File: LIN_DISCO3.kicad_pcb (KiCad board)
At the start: 2 copper layers, 38.6 x 22.6 mm, 21 parts, among them J1 Conn_01x06_Female, U1 PIC16F628-xxISO, U2 MCP1804x-5002xMB, U3 Si9243A

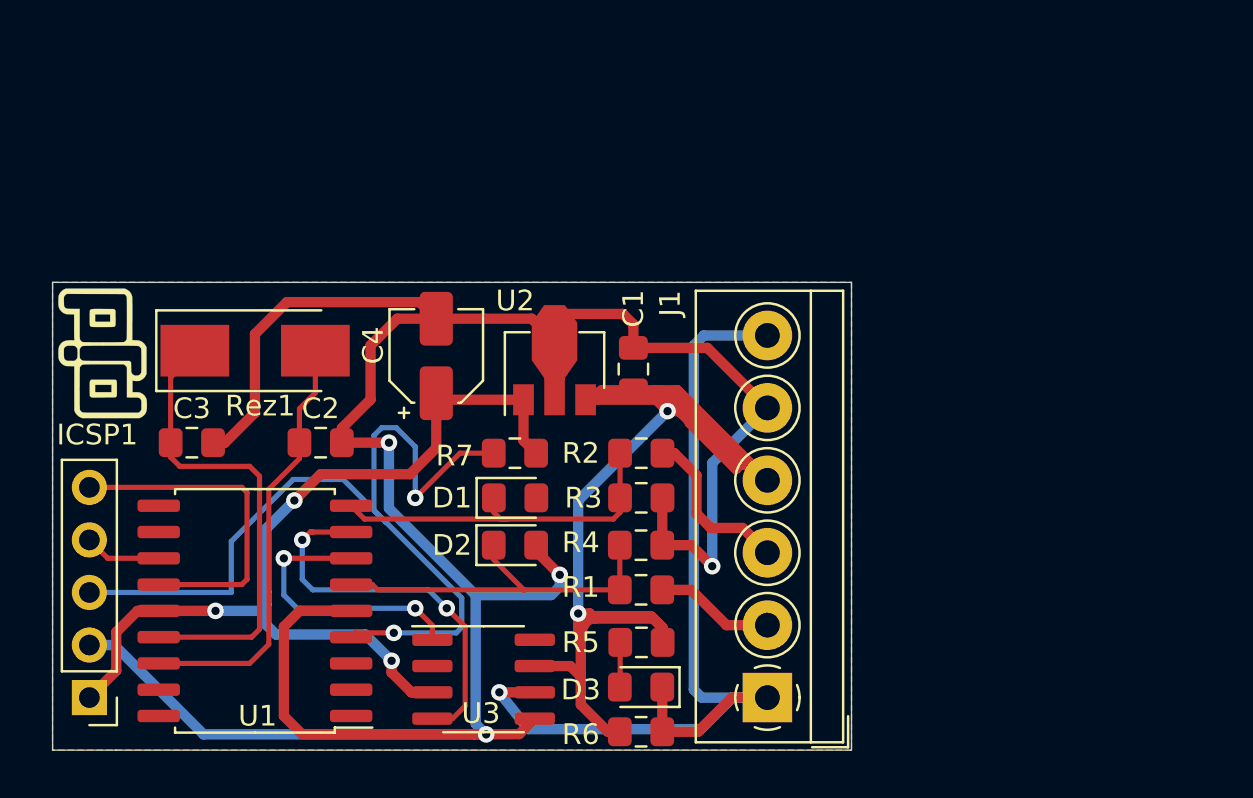
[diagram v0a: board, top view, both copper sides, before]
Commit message: design: update conn added fuse power diode bigger cappacitor
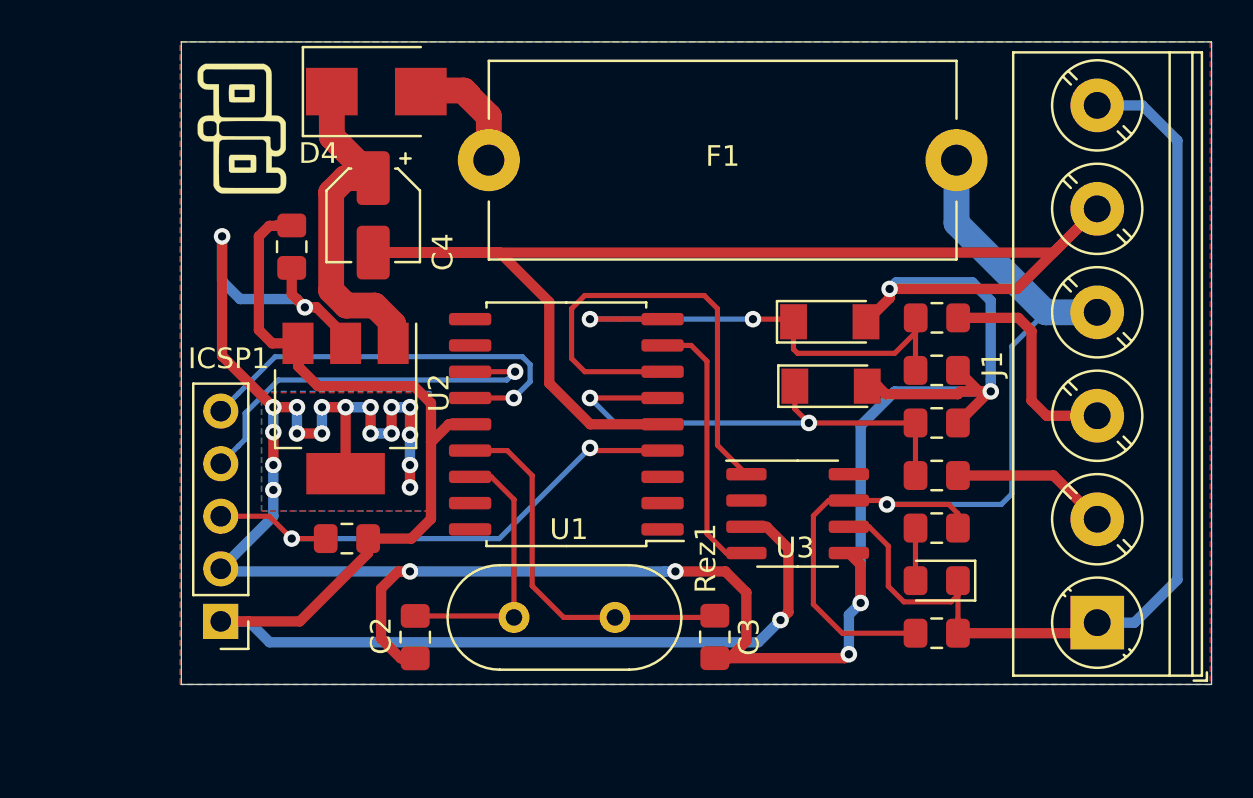
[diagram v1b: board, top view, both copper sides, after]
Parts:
- added D4: 1N4004, Diode_SMD:D_SMB, F.Cu at (171.6, 48.8)
- added F1: Fuse, Fuse:Fuseholder_Cylinder-5x20mm_Stelvio-Kontek_PTF78_Horizontal_Open, F.Cu at (177.0, 52.1)
- C4: value CP -> 10uF
- D1, D2: footprint Diode_SMD:D_0805_2012Metric_Pad1.15x1.40mm_HandSolder -> Diode_SMD:D_MiniMELF
- J1: footprint TerminalBlock_4Ucon:TerminalBlock_4Ucon_1x06_P3.50mm_Horizontal -> TerminalBlock_Phoenix:TerminalBlock_Phoenix_PT-1,5-6-5.0-H_1x06_P5.00mm_Horizontal
- Rez1: footprint Crystal:Crystal_SMD_0603-2Pin_6.0x3.5mm_HandSoldering -> Crystal:Crystal_HC49-U_Vertical
- U2: value MCP1804x-5002xMB -> MCP1825S; footprint Package_TO_SOT_SMD:SOT-89-3 -> Package_TO_SOT_SMD:SOT-223-3_TabPin2
- moved C3 27.0 mm to (188.0, 75.2), turned to 270 degrees
- moved Rez1 21.6 mm to (183.1, 74.2), turned to 180 degrees
- moved U1 17.5 mm to (180.8, 64.9)
- moved C1 17.5 mm to (167.5, 56.3), turned to 270 degrees
- moved D1 17.4 mm to (193.5, 59.9)
- moved U3 17.2 mm to (192.0, 69.2)
- moved D2 17.1 mm to (193.6, 63.1)
- moved J1 16.3 mm to (206.4, 74.5)
- moved R2 15.7 mm to (198.7, 59.8)
- moved R3 15.6 mm to (198.7, 62.3)
- moved R4 15.5 mm to (198.7, 64.8)
- moved R1 15.3 mm to (198.7, 67.4)
- moved R5 15.3 mm to (198.7, 69.9)
- moved D3 15.2 mm to (198.7, 72.5)
- moved R6 15.1 mm to (198.7, 75.0)
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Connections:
- C1 pad 1: VBAT -> Vcc
- C4 pad 1: Vcc -> Net-(C4-Pad1)
- U2 pad 1: Vcc -> Net-(C4-Pad1)
- U2 pad 3: VBAT -> Vcc
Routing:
- net GND: track 128.7 -> 201.9 mm, vias 4 -> 25
- net Vcc: track 46.2 -> 71.2 mm, vias 3 -> 1
- net Vpp: track 45.1 -> 25.3 mm
- net Net-(C4-Pad1): track 0.00 -> 16.7 mm
- net CLK: track 3.72 -> 19.0 mm, vias 0 -> 1
- net VBAT: track 59.9 -> 45.4 mm, vias 2 -> 1
- net WLINE_RX: track 13.5 -> 23.2 mm, vias 2 -> 0
- net Net-(C2-Pad1): track 20.8 -> 13.1 mm
- net RB3: track 17.7 -> 24.4 mm, vias 0 -> 2
- net RB0: track 18.0 -> 24.3 mm, vias 0 -> 2
- net WLINE_TX: track 18.9 -> 13.1 mm, vias 2 -> 0
- net Net-(D4-Pad2): track 0.00 -> 5.77 mm
- net Net-(C3-Pad1): track 22.7 -> 18.3 mm
- net DATA_IO: track 16.3 -> 20.2 mm, vias 0 -> 1
- net IGNITION: track 8.15 -> 10.7 mm
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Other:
- board size 38.6 x 22.6 mm -> 49.8 x 31.1 mm
- net class VBAT added: clearance 0.2, trace_width 1.25, via_dia 0.8, via_drill 0.4
- board text added: "8.03.22"
- board text removed: "26.01.22"
